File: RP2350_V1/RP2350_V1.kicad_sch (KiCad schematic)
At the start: 101 parts, among them IC1 DMP1045U-7, IC2 DMP1045U-7, IC3 DMP1045U-7, J1 Conn_01x04_Pin, J2 Conn_01x08_Socket, J3 USB_C_Receptacle_USB2.0_16P, J4 Conn_01x08_Socket, J5 Conn_01x08_Socket, J6 Conn_01x02_Pin, J7 Conn_01x04_Pin, SW1 PTS 647 SN50 SMTR2 LFS, SW10 PTS 647 SN50 SMTR2 LFS, SW11 PTS 647 SN50 SMTR2 LFS, SW12 PTS 647 SN50 SMTR2 LFS, SW13 PTS 647 SN50 SMTR2 LFS, SW14 PTS 647 SN50 SMTR2 LFS, SW4 PTS 647 SN50 SMTR2 LFS, SW9 PTS 647 SN50 SMTR2 LFS, U1 RP2350_60QFN, U2 W25Q128JVS, U3 TPS628110AQWRWYRQ1, U4 MCP73812T-420I-OT, U5 TLV3012AIDBVR, U6 74HC14, Y1 ASE-12.000MHZ-ET

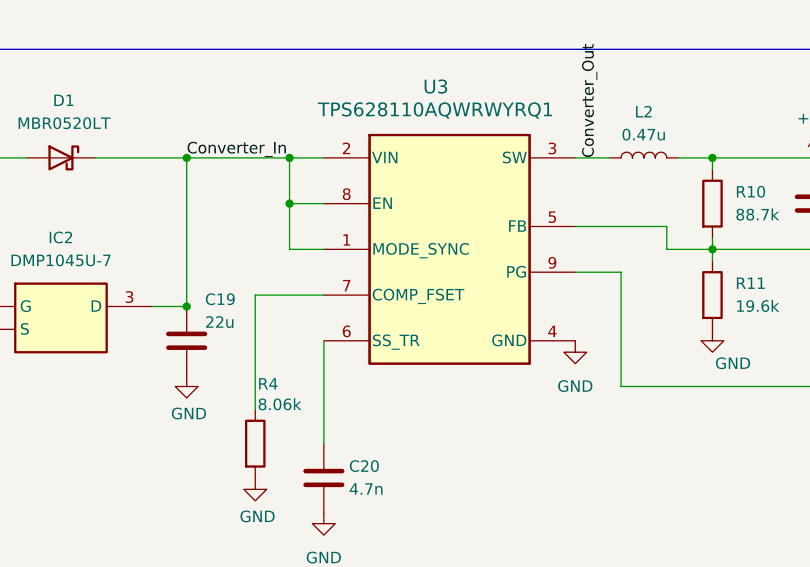
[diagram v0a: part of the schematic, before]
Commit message: DRC Clean (with waivers)
Added manual vias to RP2350 GND pad.
Silkscreen updates.
Remaining DRCs seem waivable (TPS62811 footprint bug, USB C through holes, RP2350 footprint corners)
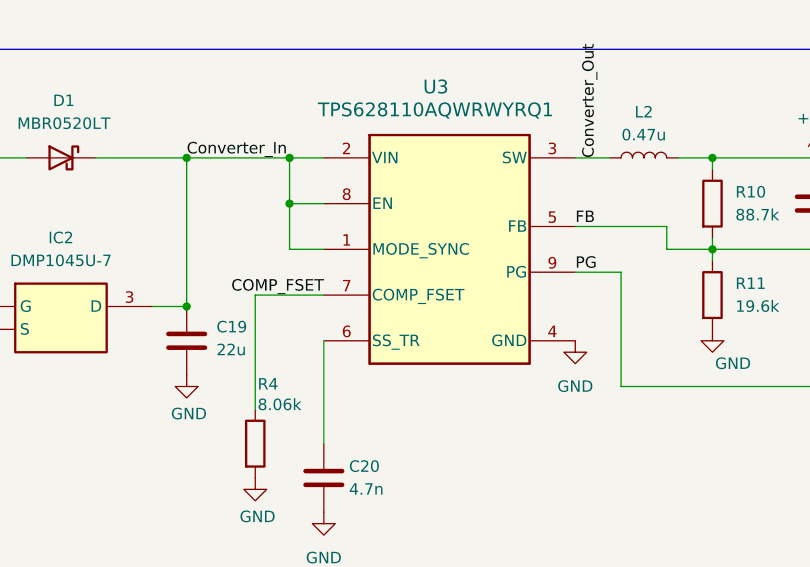
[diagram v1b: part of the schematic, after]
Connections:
- net FB: now reaches C28.2, R10.2, R11.1, U3.5 (FB)
- net COMP_FSET: now reaches R4.1, U3.7 (COMP_FSET)
- net PG: now reaches R13.2, U3.9 (PG)
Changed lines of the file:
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@@
 		)
 	)
+	(label "PG"
+		(at 257.81 236.22 0)
+		(fields_autoplaced yes)
+		(effects
+			(font
+				(size 1.27 1.27)
+			)
+			(justify left bottom)
+		)
+	)
 	(label "QSPI_SCLK"
 		(at 288.29 115.57 0)
@@
 		)
 	)
+	(label "COMP_FSET"
+		(at 229.87 238.76 180)
+		(fields_autoplaced yes)
+		(effects
+			(font
+				(size 1.27 1.27)
+			)
+			(justify right bottom)
+		)
+	)
 	(label "BTN_BACK"
 		(at 161.29 44.45 0)
@@
 		)
 	)
+	(label "FB"
+		(at 257.81 231.14 0)
+		(fields_autoplaced yes)
+		(effects
+			(font
+				(size 1.27 1.27)
+			)
+			(justify left bottom)
+		)
+	)
 	(label "SPI0_TX"
 		(at 373.38 137.16 0)
@@
 		(dnp no)
 		(property "Reference" "C19"
-			(at 216.662 239.268 0)
+			(at 217.932 242.316 0)
 			(effects
 				(font
@@
 		)
 		(property "Value" "22u"
-			(at 216.662 241.808 0)
+			(at 217.932 244.856 0)
 			(effects
 				(font

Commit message: sch updates, lay in progress
updated TLV3012 package,
changed cmos oscillator to xtal,
updated LCSC component values for all non-generic components
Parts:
- removed U5: TLV3012AIDBVR, My_Footprints:DBV6, symbol My_Library:TLV3012AIDBVR
- removed Y1: ASE-12.000MHZ-ET, My_Footprints:XTAL_ASE-12.000MHZ-ET, symbol My_Library:ASE-12.000MHZ-ET
- added C12: 15p, Capacitor_SMD:C_0402_1005Metric, symbol Device:C
- added U5: TLV3012AIDCKR, My_Footprints:DCK6, symbol My_Library:TLV3012AIDCKR
- added X1: ABM8-272-T3, My_Footprints:ABM8-272-T3_ABR, symbol My_Library:ABM8-272-T3
- C13: value 1u -> 15p
- D1: LCSC (none) -> C23848
- D2: LCSC (none) -> C605398
- D3: LCSC (none) -> C94869
- D4: LCSC (none) -> C125096
- D5: LCSC (none) -> C160478
- H1, H2, H3, H4: now left out of the parts list
- IC1, IC2, IC3: LCSC (none) -> C177033
- J1, J7: LCSC (none) -> C152150
- J2, J4: LCSC (none) -> C27438
- J3: LCSC (none) -> C165948
- J5: LCSC (none) -> C157974
- J6: LCSC (none) -> C131337
- L1: LCSC (none) -> C42411119
- L2: value 0.47u -> 560n; LCSC (none) -> C167201
- R9: value 10k -> 1k
- SW1, SW10, SW11, SW12, SW13, SW14, SW4, SW9: LCSC (none) -> C2799414
- U1: footprint My_Footprints:RP2350A_QFN-60_EP_7.75x7.75_Pitch0.4mm -> My_Footprints:RP2350-QFN-60-1EP_7x7_P0.4mm_EP3.4x3.4mm_ThermalVias_NEW; LCSC (none) -> C42411118
- U2: footprint My_Footprints:SOIC127P790X216-8N -> My_Footprints:SOIC_128JVSIQ_WIN; LCSC (none) -> C97521
- U3: value TPS628110AQWRWYRQ1 -> TPS62811QWRWYRQ1; LCSC (none) -> C2071851
- U4: LCSC (none) -> C144308
- U6: LCSC (none) -> C6820
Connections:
- net +3V3: now also U5.3 (IN+); no longer C13.1, R9.1
- net GND: now also J6.1 (Pin_1), C12.1, U5.4 (IN-), X1.2, X1.4; no longer J6.2 (Pin_2)
- net UVLO_RST: now also U5.5 (REF)
- net VBAT: now also J6.2 (Pin_2); no longer J6.1 (Pin_1)
- net XIN: now also C13.1, X1.1
- net at R29.2, R30.1: now also U5.1 (OUT)
- net XOUT: now reaches R9.2
- net XOUT: now also U1.22 (XOUT)
- new net: C12.2, R9.1, X1.3
- new net: U5.2 (V-), U5.6 (V+)
- no-connect marks 18 -> 17
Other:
- note removed: "CMOS Oscillator"
- moved on the sheet: C13, J6, R9

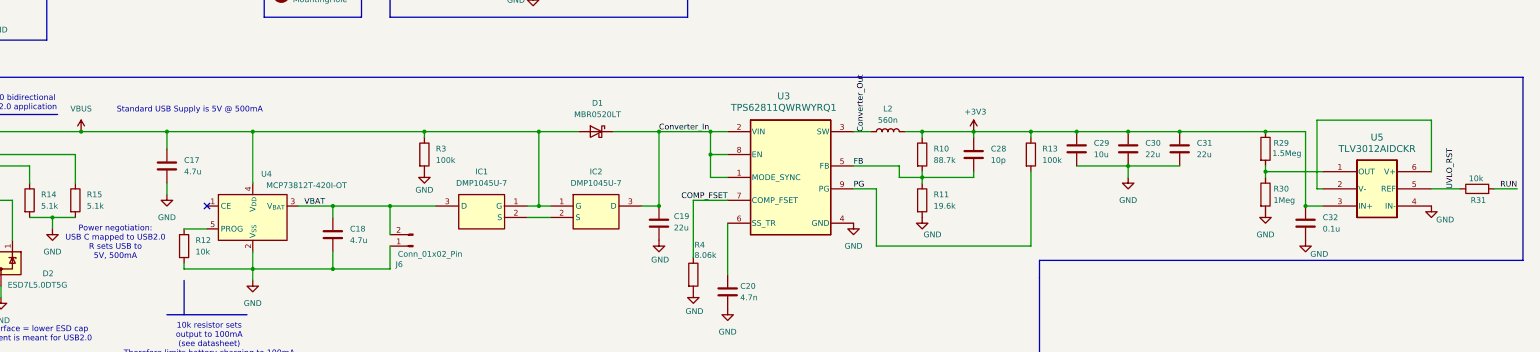
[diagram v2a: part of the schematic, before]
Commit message: DONOT USE PREVIOUS VERSIONS! *Fixed TLV3012*, added TVS diodes
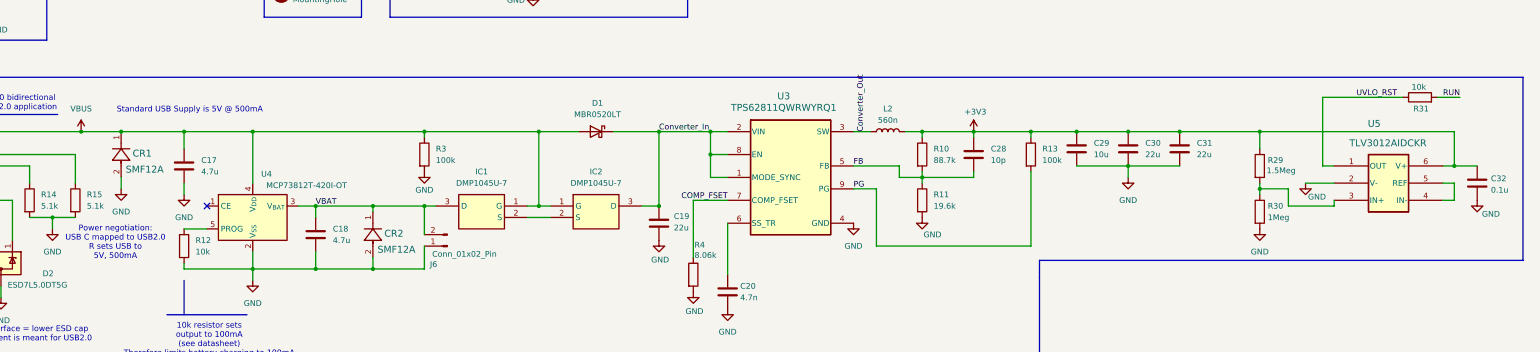
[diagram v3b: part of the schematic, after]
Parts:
- added CR1, CR2: SMF12A, My_Footprints:SMFSeries_SOD-123F, symbol My_Library:SMF12A
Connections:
- net +3V3: now also U5.6 (V+); no longer U5.3 (IN+)
- net GND: now also U5.2 (V-), CR1.2, CR2.2; no longer U5.4 (IN-)
- net UVLO_RST: now also U5.1 (OUT); no longer U5.5 (REF)
- net VBAT: now also CR2.1
- net VBUS: now also CR1.1
- net at R29.2, R30.1: now also U5.3 (IN+); no longer U5.1 (OUT)
- new net: U5.4 (IN-), U5.5 (REF)
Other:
- moved on the sheet: C17, C18, C32, J6, R29, R30, R31, U5

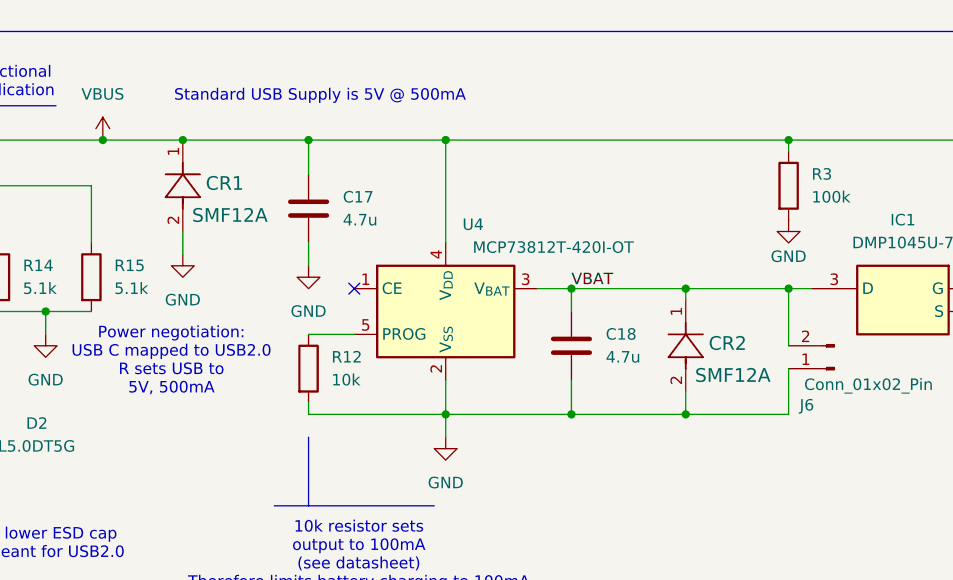
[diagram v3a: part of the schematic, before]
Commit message: Updated TVS diode to bi-directional version (SMF12CA)
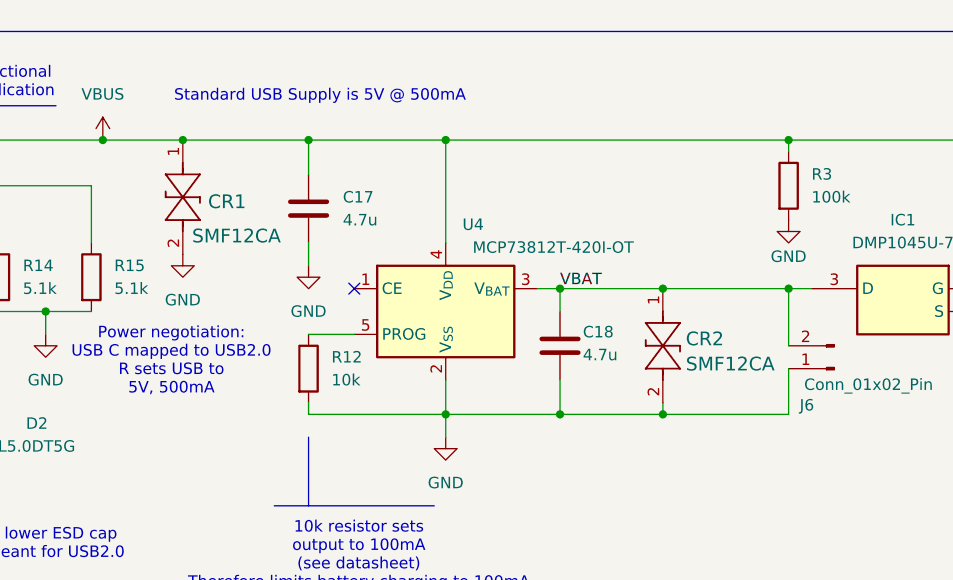
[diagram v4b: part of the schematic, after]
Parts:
- removed CR1, CR2: SMF12A, My_Footprints:SMFSeries_SOD-123F, symbol My_Library:SMF12A
- added CR1, CR2: SMF12CA, My_Footprints:SMFSeries_SOD-123F, symbol My_Library:SMF12CA
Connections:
- net GND: now also CR1.2, CR2.2
- net VBAT: now also CR2.1
- net VBUS: now also CR1.1
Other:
- moved on the sheet: C18

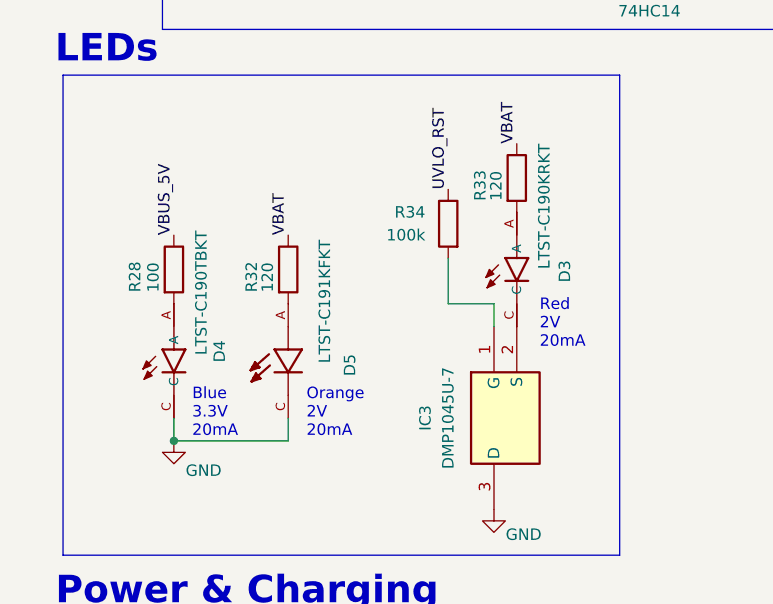
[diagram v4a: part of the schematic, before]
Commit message: updated LED resistors, re-exported fabrication outputs
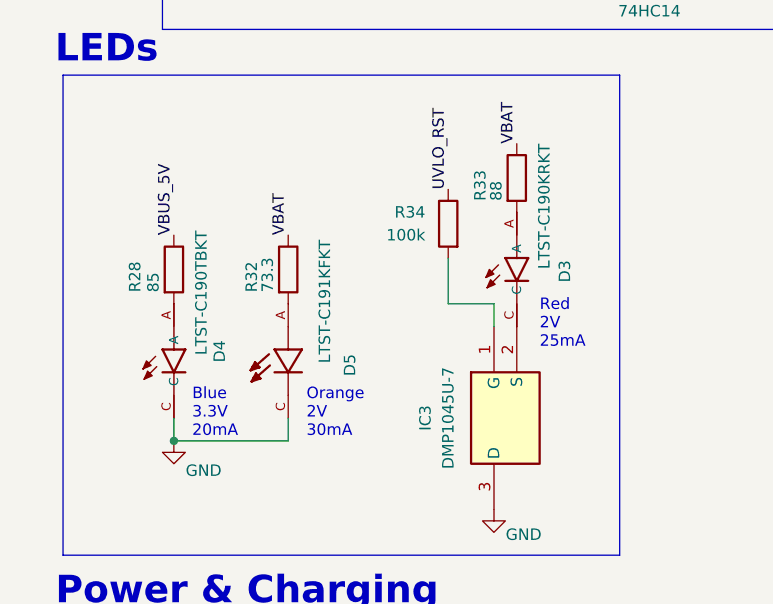
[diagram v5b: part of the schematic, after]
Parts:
- R28: value 100 -> 85
- R32: value 120 -> 73.3
- R33: value 120 -> 88
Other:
- note added: "Orange 2V 30mA"
- note added: "Red 2V 25mA"
- note removed: "Orange 2V 20mA"
- note removed: "Red 2V 20mA"
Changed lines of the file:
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@@
 		)
 	)
-	(text "Orange\n2V\n20mA"
+	(text "Orange\n2V\n30mA"
 		(exclude_from_sim no)
 		(at 43.942 187.452 0)
@@
 		)
 	)
-	(text "Red\n2V\n20mA"
+	(text "Red\n2V\n25mA"
 		(exclude_from_sim no)
 		(at 69.85 177.546 0)
@@
 			)
 		)
-		(property "Value" "120"
+		(property "Value" "73.3"
 			(at 39.624 173.99 90)
 			(effects
@@
 			)
 		)
-		(property "Value" "100"
+		(property "Value" "85"
 			(at 26.924 173.99 90)
 			(effects
@@
 			)
 		)
-		(property "Value" "120"
+		(property "Value" "88"
 			(at 65.024 163.83 90)
 			(effects

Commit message: caps added
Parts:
- C1, C10, C11, C14, C16, C21, C22, C23, C24, C25, C26, C27, C32, C5, C6, C7, C8, C9: LCSC (none) -> C1525
- C12, C13: LCSC (none) -> C86285
- C15, C2, C3, C4: LCSC (none) -> C23733
- C17, C18: LCSC (none) -> C1746
- C19, C30, C31: LCSC (none) -> C5674
- C20: LCSC (none) -> C84705
- C28: LCSC (none) -> C32949
- C29: LCSC (none) -> C1713

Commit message: Rs added
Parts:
- R1, R2, R9: LCSC (none) -> C11702
- R10: LCSC (none) -> C25922
- R11: LCSC (none) -> C26959
- R12, R16, R17, R18, R19, R20, R21, R22, R23, R24, R25, R26, R27, R31, R5: LCSC (none) -> C25744
- R14, R15: LCSC (none) -> C25905
- R29: LCSC (none) -> C11812
- R30: LCSC (none) -> C26083
- R6: LCSC (none) -> C25105
- R7, R8: LCSC (none) -> C25100

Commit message: try again for BOM?
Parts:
- CR1, CR2: LCSC (none) -> C123801
- R13, R3, R34: LCSC (none) -> C25530
- R28: value 85 -> 86.6; LCSC (none) -> C270575
- R32: value 73.3 -> 75; LCSC (none) -> C25133
- R33: value 88 -> 88.7; LCSC (none) -> C423126
- R4: LCSC (none) -> C25923
